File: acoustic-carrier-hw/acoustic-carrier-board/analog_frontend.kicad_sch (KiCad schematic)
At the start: 62 parts, among them J1 8P8C_Shielded, J10 BWU.FL-IPEX1, J11 BWU.FL-IPEX1, J12 BWU.FL-IPEX1, J13 BWU.FL-IPEX1, J14 BWU.FL-IPEX1, J5 BWU.FL-IPEX1, J7 BWU.FL-IPEX1, U13 TL432DBZ, U2 THS4521IDGK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

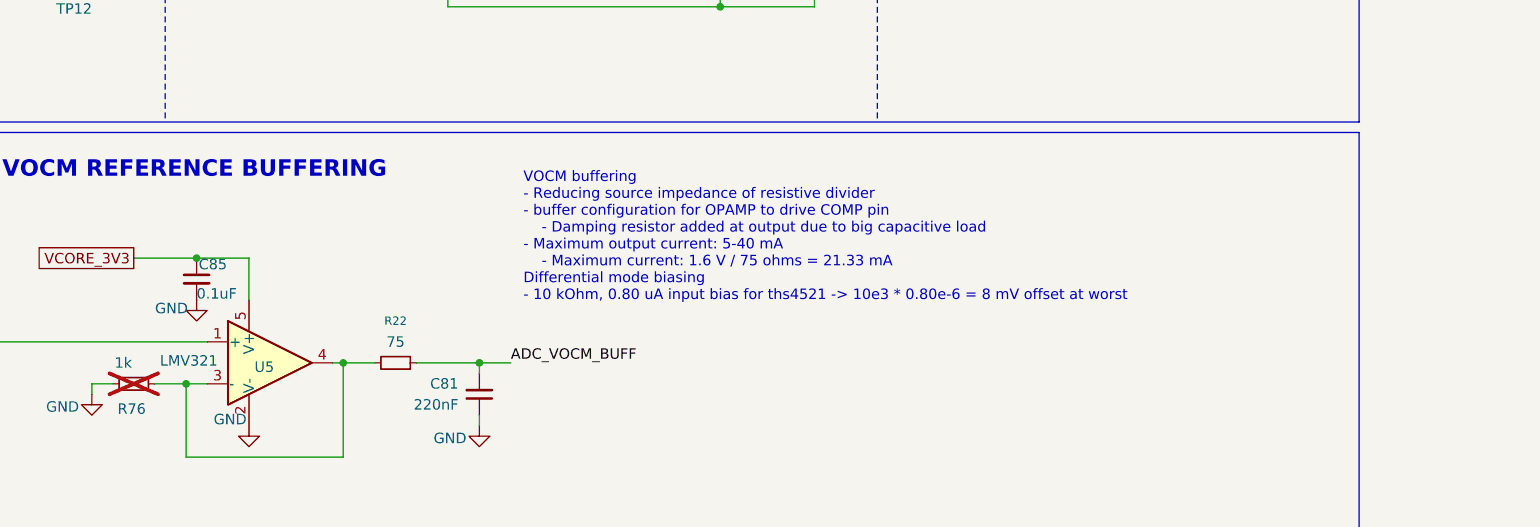
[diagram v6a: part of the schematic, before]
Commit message: [carrier] Added precision amplifier for DDRL voltage reference
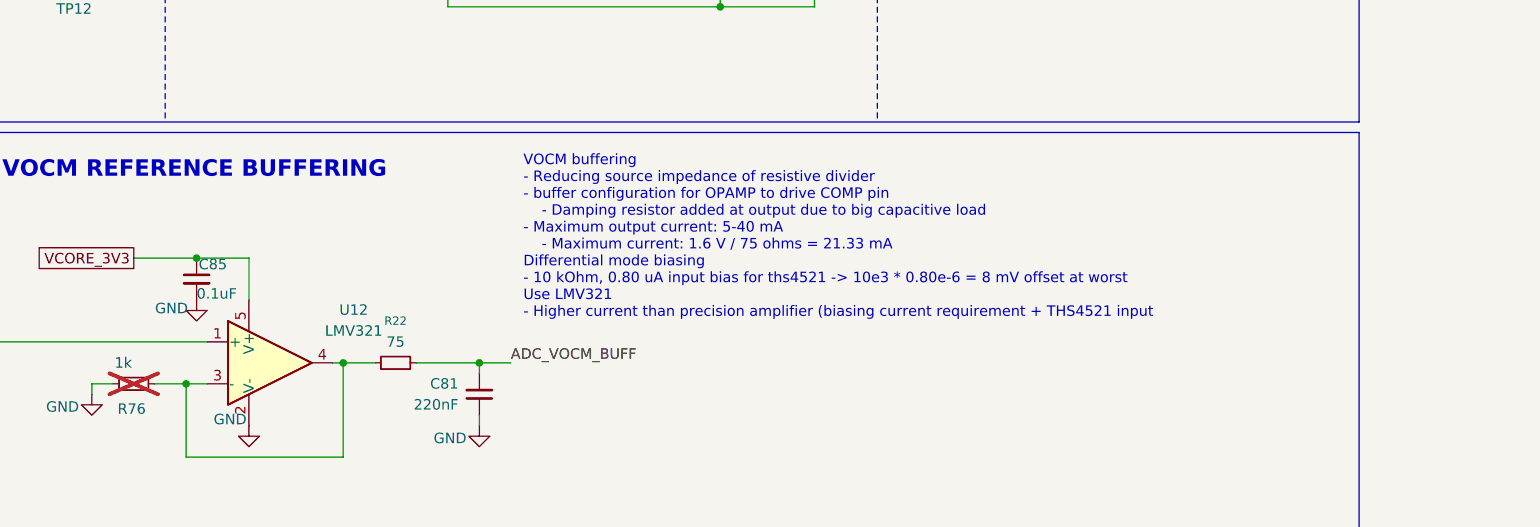
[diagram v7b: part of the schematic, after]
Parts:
- removed U5: LMV321, Package_TO_SOT_SMD:SOT-23-5, symbol Amplifier_Operational:LMV321
- added U12: LMV321, Package_TO_SOT_SMD:SOT-23-5, symbol Amplifier_Operational:LMV321
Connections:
- net ADC_VOCM_REF: now also U12.1 (+)
- net GND: now also U12.2 (V-)
- net VCORE_3V3: now also U12.5 (V+)
- net at R22.2, R76.2: now also U12.3 (-), U12.4
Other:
- note added: "VOCM buffering - Reducing source impedance of resistive divider - buffer configuration for OPAMP to drive COMP pin - Damping resistor added at output due to big capacitive load - Maximum output current: 5-40 mA - Maximum current: 1.6 V / 75 ohms = 21.33 mA Differential mode biasing - 10 kOhm, 0.80 uA input bias for ths4521 -> 10e3 * 0.80e-6 = 8 mV offset at worst Use LMV321 - Higher current than 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"
- note removed: "VOCM buffering - Reducing source impedance of resistive divider - buffer configuration for OPAMP to drive COMP pin - Damping resistor added at output due to big capacitive load - Maximum output current: 5-40 mA - Maximum current: 1.6 V / 75 ohms = 21.33 mA Differential mode biasing - 10 kOhm, 0.80 uA input bias for ths4521 -> 10e3 * 0.80e-6 = 8 mV offset at worst"
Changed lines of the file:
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@@
 		)
 	)
-	(text "VOCM buffering\n- Reducing source impedance of resistive divider\n- buffer configuration for OPAMP to drive COMP pin\n	- Damping resistor added at output due to big capacitive load\n- Maximum output current: 5-40 mA\n	- Maximum current: 1.6 V / 75 ohms = 21.33 mA\nDifferential mode biasing\n- 10 kOhm, 0.80 uA input bias for ths4521 -> 10e3 * 0.80e-6 = 8 mV offset at worst"
+	(text "VOCM buffering\n- Reducing source impedance of resistive divider\n- buffer configuration for OPAMP to drive COMP pin\n	- Damping resistor added at output due to big capacitive load\n- Maximum output current: 5-40 mA\n	- Maximum current: 1.6 V / 75 ohms = 21.33 mA\nDifferential mode biasing\n- 10 kOhm, 0.80 uA input bias for ths4521 -> 10e3 * 0.80e-6 = 8 mV offset at worst\nUse LMV321\n- Higher current than precision amplifier (biasing current requirement + THS4521 input"
 		(exclude_from_sim no)
 		(at 181.864 125.73 0)
@@
 	)
 	(symbol
+		(lib_id "Amplifier_Operational:LMV321")
+		(at 151.13 140.97 0)
+		(unit 1)
+		(exclude_from_sim no)
+		(in_bom yes)
+		(on_board yes)
+		(dnp no)
+		(fields_autoplaced yes)
+		(property "Reference" "U12"
+			(at 161.29 134.5498 0)
+			(effects
+				(font
+					(size 1.27 1.27)
+				)
+			)
+		)
+		(property "Value" "LMV321"
+			(at 161.29 137.0898 0)
+			(effects
+				(font
+					(size 1.27 1.27)
+				)
+			)
+		)
+		(property "Footprint" "Package_TO_SOT_SMD:SOT-23-5"
+			(at 151.13 140.97 0)
+			(effects
+				(font
+					(size 1.27 1.27)
+				)
+				(justify left)
+				(hide yes)
+			)
+		)
+		(property "Datasheet" "http://www.ti.com/lit/ds/symlink/lmv324.pdf"
+			(at 151.13 140.97 0)
+			(effects
+				(font
+					(size 1.27 1.27)
+				)
+				(hide yes)
+			)
+		)
+		(property "Description" "Low-Voltage Rail-to-Rail Output Operational Amplifiers, SOT-23-5/SC-70-5"
+			(at 151.13 140.97 0)
+			(effects
+				(font
+					(size 1.27 1.27)
+				)
+				(hide yes)
+			)
+		)
+		(property "LPN" "C7972"
+			(at 151.13 140.97 0)
+			(effects
+				(font
+					(size 1.27 1.27)
+				)
+				(hide yes)
+			)
+		)
+		(property "MPN" "LMV321IDBVR"
+			(at 151.13 140.97 0)
+			(effects
+				(font
+					(size 1.27 1.27)
+				)
+				(hide yes)
+			)
+		)
+		(pin "2"
+		)
+		(pin "3"
+		)
+		(pin "1"
+		)
+		(pin "5"
+		)
+		(pin "4"
+		)
+		(instances
+			(project ""
+				(path "/25b015c9-ab13-4427-b72c-b6f348597100/2e3c577d-8737-43a3-b422-36e75ce65de9"
+					(reference "U12")
+					(unit 1)
+				)
+			)
+		)
+	)
+	(symbol
 		(lib_id "Device:C_Small")
 		(at 44.45 96.52 90)
@@
 					(unit 1)
 				)
-			)
-		)
-	)
-	(symbol
-		(lib_id "Amplifier_Operational:LMV321")
-		(at 151.13 140.97 0)
-		(unit 1)
-		(exclude_from_sim no)
-		(in_bom yes)
-		(on_board yes)
-		(dnp no)
-		(property "Reference" "U5"
-			(at 151.638 141.478 0)
-			(effects
-				(font
-					(size 1.27 1.27)
-				)
-				(justify right)
-			)
-		)
-		(property "Value" "LMV321"
-			(at 144.78 140.716 0)
-			(effects
-				(font
-					(size 1.27 1.27)
-				)
-				(justify right)
-			)
-		)
-		(property "Footprint" "Package_TO_SOT_SMD:SOT-23-5"
-			(at 151.13 140.97 0)
-			(effects
-				(font
-					(size 1.27 1.27)
-				)
-				(justify left)
-				(hide yes)
-			)
-		)
-		(property "Datasheet" "http://www.ti.com/lit/ds/symlink/lmv324.pdf"
-			(at 151.13 140.97 0)
-			(effects
-				(font
-					(size 1.27 1.27)
-				)
-				(hide yes)
-			)
-		)
-		(property "Description" "Low-Voltage Rail-to-Rail Output Operational Amplifiers, SOT-23-5/SC-70-5"
-			(at 151.13 140.97 0)
-			(effects
-				(font
-					(size 1.27 1.27)
-				)
-				(hide yes)
-			)
-		)
-		(property "LPN" "C7972"
-			(at 151.13 140.97 0)
-			(effects
-				(font
-					(size 1.27 1.27)
-				)
-				(hide yes)
-			)
-		)
-		(property "MPN" "LMV321IDBVR"
-			(at 151.13 140.97 0)
-			(effects
-				(font
-					(size 1.27 1.27)
-				)
-				(hide yes)
-			)
-		)
-		(pin "2"
-		)
-		(pin "4"
-		)
-		(pin "3"
-		)
-		(pin "1"
-		)
-		(pin "5"
-		)
-		(instances
-			(project ""
-				(path "/25b015c9-ab13-4427-b72c-b6f348597100/2e3c577d-8737-43a3-b422-36e75ce65de9"
-					(reference "U5")
-					(unit 1)
-				)

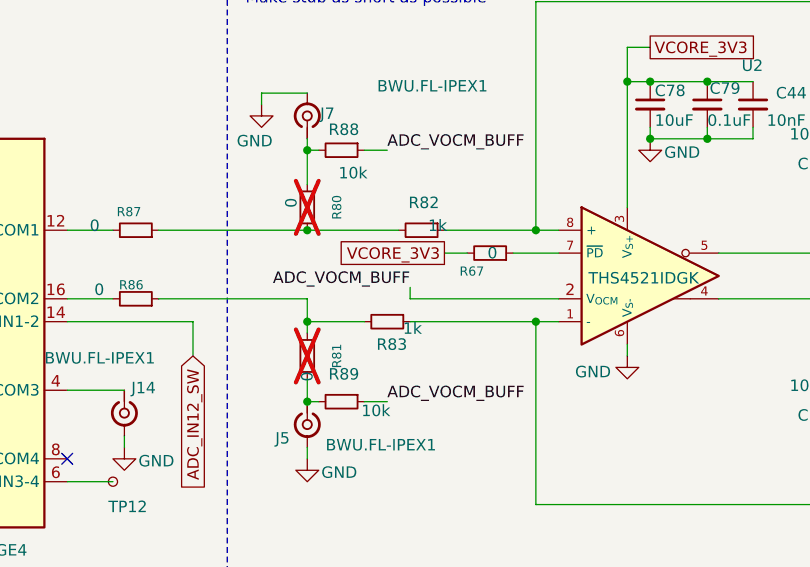
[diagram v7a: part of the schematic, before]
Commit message: [carrier] Worked on USB connector
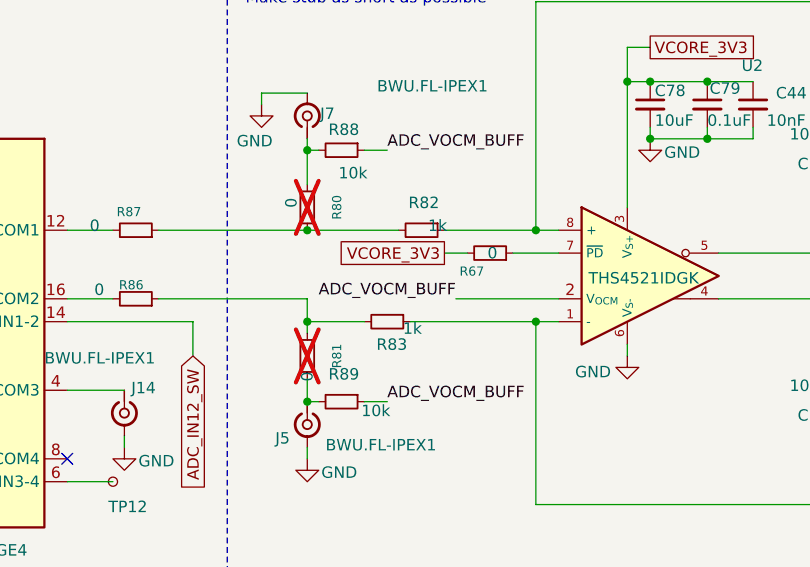
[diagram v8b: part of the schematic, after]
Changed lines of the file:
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@@
 	(wire
 		(pts
-			(xy 158.75 74.93) (xy 175.26 74.93)
+			(xy 163.83 74.93) (xy 175.26 74.93)
 		)
 		(stroke
@@
 	(wire
 		(pts
-			(xy 158.75 73.66) (xy 158.75 74.93)
-		)
-		(stroke
-			(width 0)
-			(type default)
-		)
-	)
-	(wire
-		(pts
 			(xy 193.04 74.93) (xy 205.74 74.93)
 		)
@@
 	)
 	(label "ADC_VOCM_BUFF"
-		(at 158.75 73.66 180)
+		(at 163.83 74.93 180)
 		(effects
 			(font
